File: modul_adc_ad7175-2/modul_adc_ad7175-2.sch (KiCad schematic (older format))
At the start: 84 parts

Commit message: Подготовил печатную плату к разводке.
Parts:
- removed C?: 270 п, symbol CAPITORS
- removed C?: 0.1 мк, symbol CAPITORS
- removed C?: 22 п, symbol CAPITORS
- removed C?: 1 мк, symbol CAPITORS
- removed DA?: OP07, symbol OP07
- removed R? (x4): 0, symbol RESISTOR
- removed R?: 10, symbol RESISTOR
- removed R? (x2): 10 к, symbol RESISTOR
- removed R?: 1 к, symbol RESISTOR
- removed XP?: WF-5, symbol PIN_M_5
- removed XP?: WF-6, symbol PIN_M_6
- removed XP?: SMA-JR, symbol PIN_F_5
- added R24, R25, R26, R27: 0, IWsmd_case:SMD0805, symbol RESISTOR
- added XP1, XP2: PLS-8, IWconnectors:PIN_ARRAY_8x1, symbol PIN_M_8
- added XP3, XP4: PLS-6, IWconnectors:PIN_ARRAY_6x1, symbol PIN_M_6
- C1, C10, C11, C12, C13, C14, C15, C16, C17, C18, C2, C21, C22, C23, C24, C25, C28, C29, C3, C4, C7, C8, C9: renamed from C?; footprint (none) -> IWsmd_case:SMD0805
- C19, C20: renamed from C?; value 12 п -> 9.1 п; footprint (none) -> IWsmd_case:SMD0805
- C26, C27, C5, C6: renamed from C?; footprint (none) -> IWsmd_case:CASE_B
- DA1, DA2: renamed from DA?; footprint (none) -> IWsmd_case:MSOP-10
- DA3: renamed from DA?; footprint (none) -> IWsmd_case:SOIC8
- DD1: renamed from DD?; footprint (none) -> IWsmd_case:TSOP24
- R1, R10, R11, R12, R13, R2, R22, R23, R28, R29, R3, R30, R31, R34, R35, R4, R5, R6, R7, R8, R9: renamed from R?; footprint (none) -> IWsmd_case:SMD0805
- R14, R15, R16, R17, R18, R19, R20, R21: renamed from R?; value 5 к -> 5 к 0.1%; footprint (none) -> IWsmd_case:SMD0805
- R32, R33: renamed from R?; value 10 к -> 10 к 0.1%; footprint (none) -> IWsmd_case:SMD0805
- XP5: renamed from XP?; footprint (none) -> IWconnectors:WF-3
- XP6, XP7: renamed from XP?; footprint (none) -> IWconnectors:SMA-R
- Z1: value 16 МГц -> FA-20H 16 МГц; footprint (none) -> IWsmd_case:EPSON_FA-20H
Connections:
- net REF- is gone; now on net AGND: C17.1, DD1.2 (REF-)
- net AGND: now also R25.2
- net AVCC: now also R26.1
- net DGND: now also R27.1
- net DVCC: now also R24.2
- net GND: now also R25.1, R27.2, XP3.4, XP3.5
- net MOSI: now also R8.2; no longer R10.2
- net REF+: now also C7.2, C8.2, DA3.6 (Vout)
- net SCLK: now also R10.2; no longer R7.2
- net ~CS: now also R7.2; no longer R11.2
- net ~SYNC~/ERR: now also R11.2; no longer R8.2
- net A5: now reaches R11.1
- net A5: now also XP4.6
- net PB2: now reaches R7.1
- net PB2: now also XP1.3
- net PB5: now reaches R10.1
- net PB5: now also XP1.6
- net PB4: now reaches R9.1
- net PB4: now also XP1.5
- net PB3: now reaches R8.1
- net PB3: now also XP1.4
- new net +5V: R24.1, R26.2, XP3.3
- new net A0: XP4.1
- new net A1: XP4.2
- new net A2: XP4.3
- new net A3: XP4.4
- new net A4: XP4.5
- new net PB0: XP1.1
- new net PB1: XP1.2
- new net PD4: XP2.5
- new net PD5: XP2.6
- new net PD6: XP2.7
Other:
- note added: "Источник питания от 6 до 18 В\nдля источника опроного напряжения\nиспользуется только только для ADR445BRZ"
- note removed: "Источник питания от 6 до 18 В\nдля источника опроного напряжения\nиспользуется только только для ADR445"
- moved on the sheet: C1, C10, C11, C12, C13, C14, C15, C2, C3, C4, C5, C6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

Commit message: Приступил к разводке платы c AD7175-2.
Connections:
- net A5: no longer R11.1
- net AGND: now also XP5.1; no longer XP5.3
- net PB1: now also R11.1
- net VCC_REF: now also XP5.3; no longer XP5.1
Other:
- moved on the sheet: R11
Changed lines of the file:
@@
 L RESISTOR R11
 U 1 1 5A7C8168
-P 1550 9100
-F 0 "R11" H 1550 9200 71  0000 C CNN
-F 1 "0" H 1800 9200 71  0000 C CNN
-F 2 "IWsmd_case:SMD0805" H 1550 9100 60  0001 C CNN
-F 3 "" H 1550 9100 60  0000 C CNN
-	1    1550 9100
+P 1650 6450
+F 0 "R11" H 1650 6550 71  0000 C CNN
+F 1 "0" H 1900 6550 71  0000 C CNN
+F 2 "IWsmd_case:SMD0805" H 1650 6450 60  0001 C CNN
+F 3 "" H 1650 6450 60  0000 C CNN
+	1    1650 6450
 	1    0    0    -1
 $EndComp
@@
 	3900 2000 3800 2000
 Wire Wire Line
-	3800 2000 3800 2250
-Wire Wire Line
-	3800 2250 3100 2250
+	3800 2250 3800 2000
+Wire Wire Line
+	3100 2250 3800 2250
 Wire Wire Line
 	3100 2150 3100 2550
@@
 L PIN_M_3 XP5
 U 1 1 5AA14678
-P 1150 1800
-F 0 "XP5" H 1300 2000 50  0000 L BNN
-F 1 "WF-3" H 1250 1900 50  0000 L BNN
-F 2 "IWconnectors:WF-3" H 1600 1950 50  0001 C CNN
-F 3 "" H 1150 1800 60  0000 C CNN
-	1    1150 1800
-	-1   0    0    -1
+P 1150 2000
+F 0 "XP5" H 1350 1550 50  0000 L BNN
+F 1 "WF-3" H 1300 1650 50  0000 L BNN
+F 2 "IWconnectors:WF-3" H 1600 2150 50  0001 C CNN
+F 3 "" H 1150 2000 60  0000 C CNN
+	1    1150 2000
+	-1   0    0    1
 $EndComp
 Text Label 1600 1800 2    60   ~ 0
@@
 PB0
 Wire Wire Line
-	1100 6600 1350 6600
+	1100 6600 1450 6600
 Text Label 1350 6600 2    60   ~ 0
 PB1
@@
 Text Label 1350 8150 2    60   ~ 0
 PD6
-Text Label 2250 6650 2    60   ~ 0
+Text Label 2500 6650 2    60   ~ 0
 ~CS
-Text Label 2250 7250 2    60   ~ 0
+Text Label 2500 7250 2    60   ~ 0
 SCLK
-Text Label 2250 6850 2    60   ~ 0
+Text Label 2500 6850 2    60   ~ 0
 MOSI
-Text Label 2250 7050 2    60   ~ 0
+Text Label 2500 7050 2    60   ~ 0
 MISO
-Text Label 2400 9100 2    60   ~ 0
+Text Label 2500 6450 2    60   ~ 0
 ~SYNC~/ERR
 Wire Wire Line
-	1800 9100 2400 9100
-Wire Wire Line
-	1900 6650 2250 6650
-Wire Wire Line
-	1900 7250 2250 7250
+	1900 6450 2500 6450
+Wire Wire Line
+	1900 6650 2500 6650
+Wire Wire Line
+	1900 7250 2500 7250
 Wire Wire Line
 	1100 7000 1450 7000
@@
 	1450 7250 1650 7250
 Wire Wire Line
-	1900 7050 2250 7050
+	1900 7050 2500 7050
 Wire Wire Line
 	1500 6900 1500 7050
@@
 	1500 7050 1650 7050
 Wire Wire Line
-	1900 6850 2250 6850
+	1900 6850 2500 6850
 Wire Wire Line
 	1550 6800 1550 6850
@@
 	6100 1450 6600 1450
 Wire Wire Line
-	1100 9100 1550 9100
+	1450 6600 1450 6450
+Wire Wire Line
+	1450 6450 1650 6450
+Wire Wire Line
+	1100 9100 1350 9100
 $EndSCHEMATC

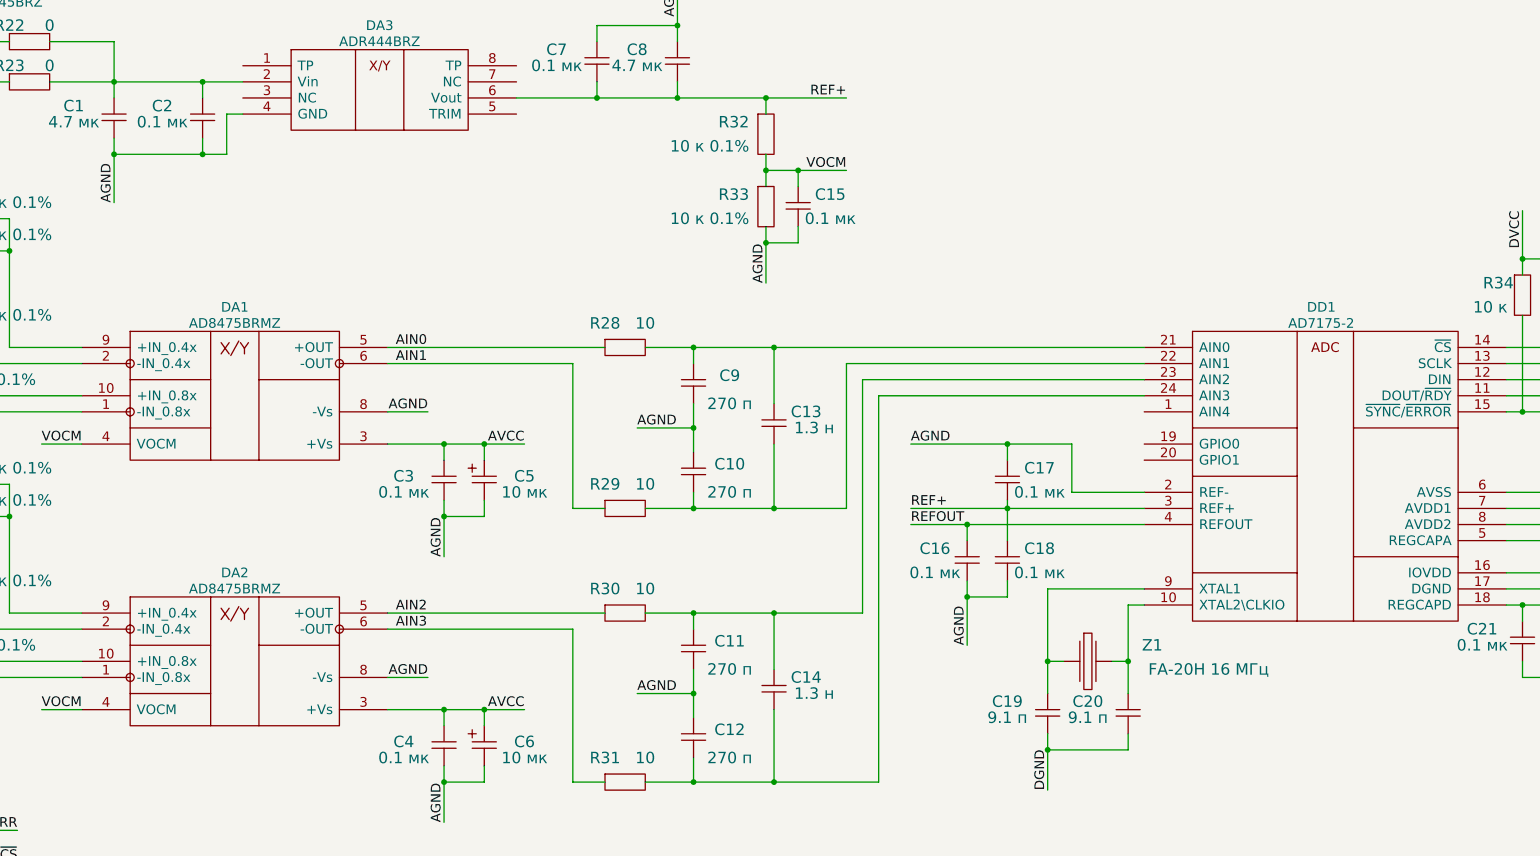
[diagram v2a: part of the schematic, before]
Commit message: Закончил разводку платы c AD7175-2.
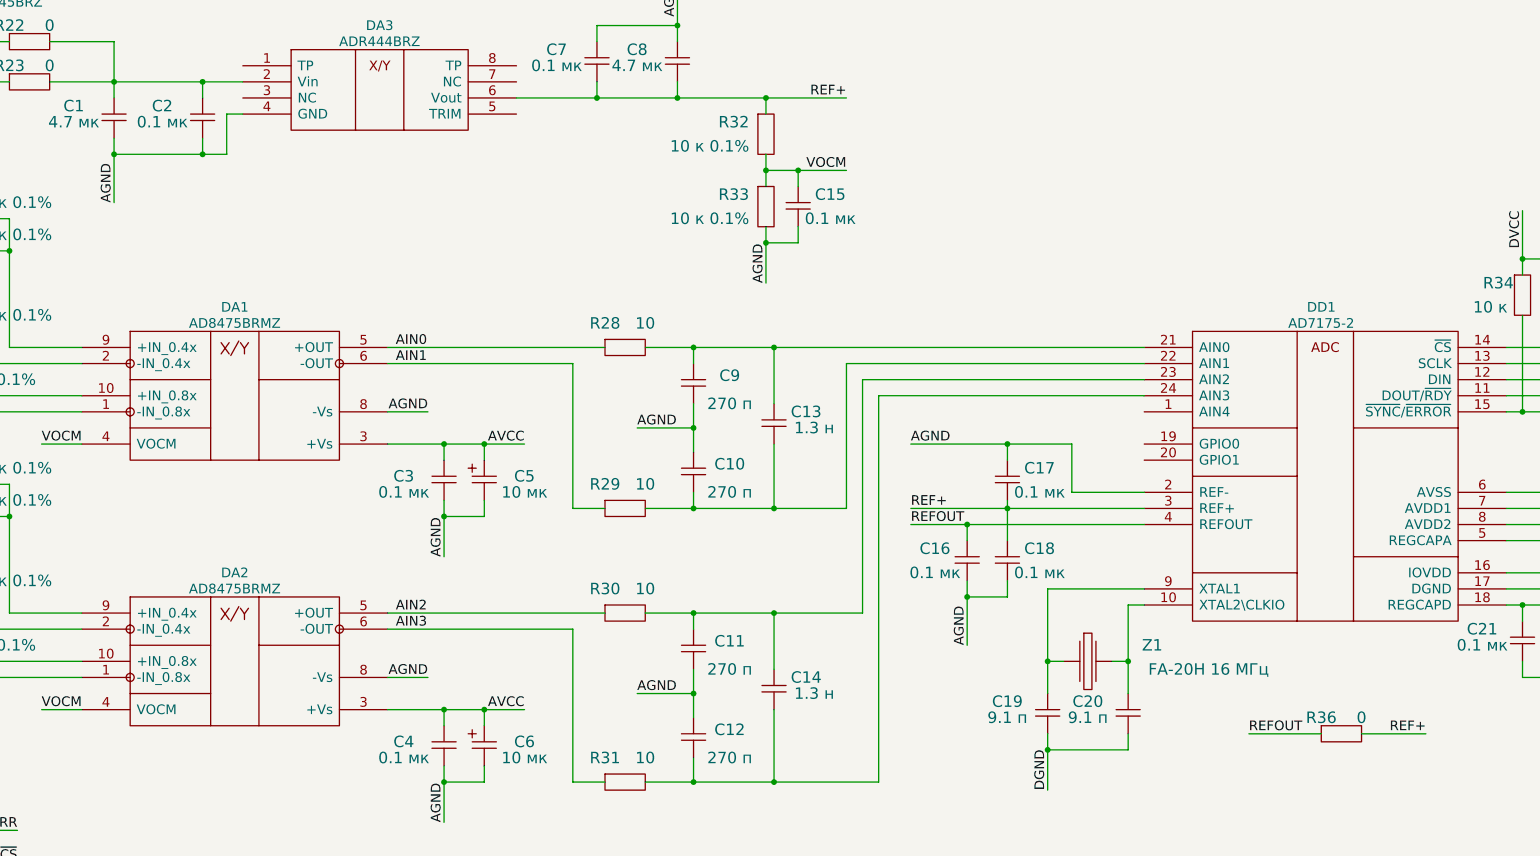
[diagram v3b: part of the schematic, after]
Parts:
- added R36: 0, IWsmd_case:SMD0805, symbol RESISTOR
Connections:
- net REF+: now also R36.2
- net REFOUT: now also R36.1
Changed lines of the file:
@@
 	3900 2000 3800 2000
 Wire Wire Line
-	3800 2250 3800 2000
-Wire Wire Line
-	3100 2250 3800 2250
+	3800 2000 3800 2250
+Wire Wire Line
+	3800 2250 3100 2250
 Wire Wire Line
 	3100 2150 3100 2550
@@
 Wire Wire Line
 	1100 9100 1350 9100
+$Comp
+L RESISTOR R36
+U 1 1 5AD0D680
+P 10600 5850
+F 0 "R36" H 10600 5950 71  0000 C CNN
+F 1 "0" H 10850 5950 71  0000 C CNN
+F 2 "IWsmd_case:SMD0805" H 10600 5850 60  0001 C CNN
+F 3 "" H 10600 5850 60  0000 C CNN
+	1    10600 5850
+	1    0    0    -1
+$EndComp
+Text Label 10150 5850 0    60   ~ 0
+REFOUT
+Wire Wire Line
+	10150 5850 10600 5850
+Wire Wire Line
+	10850 5850 11250 5850
+Text Label 11250 5850 2    60   ~ 0
+REF+
 $EndSCHEMATC

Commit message: Добавил номиналы резисторов подключенных последовательно SPI для АЦП AD7175-2.
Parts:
- R10, R7, R8, R9: value 0 -> 33
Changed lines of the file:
@@
 P 1650 6850
 F 0 "R8" H 1650 6950 71  0000 C CNN
-F 1 "0" H 1900 6950 71  0000 C CNN
+F 1 "33" H 1900 6950 71  0000 C CNN
 F 2 "IWsmd_case:SMD0805" H 1650 6850 60  0001 C CNN
 F 3 "" H 1650 6850 60  0000 C CNN
@@
 P 1650 7050
 F 0 "R9" H 1650 7150 71  0000 C CNN
-F 1 "0" H 1900 7150 71  0000 C CNN
+F 1 "33" H 1900 7150 71  0000 C CNN
 F 2 "IWsmd_case:SMD0805" H 1650 7050 60  0001 C CNN
 F 3 "" H 1650 7050 60  0000 C CNN
@@
 P 1650 7250
 F 0 "R10" H 1650 7350 71  0000 C CNN
-F 1 "0" H 1900 7350 71  0000 C CNN
+F 1 "33" H 1900 7350 71  0000 C CNN
 F 2 "IWsmd_case:SMD0805" H 1650 7250 60  0001 C CNN
 F 3 "" H 1650 7250 60  0000 C CNN
@@
 P 1650 6650
 F 0 "R7" H 1650 6750 71  0000 C CNN
-F 1 "0" H 1900 6750 71  0000 C CNN
+F 1 "33" H 1900 6750 71  0000 C CNN
 F 2 "IWsmd_case:SMD0805" H 1650 6650 60  0001 C CNN
 F 3 "" H 1650 6650 60  0000 C CNN
